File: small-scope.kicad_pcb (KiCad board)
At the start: 2 copper layers, 35.6 x 53.3 mm, 41 parts, among them P1 BNC, P2 AREF, SW1 STAT DIS, U1 LM324N

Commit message: initial placement
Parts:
- C5: value 16.9p -> 16p
- C7: value 135p -> 130p
- R1, R3, R4, R5, R6, R7, R8: footprint R4-LARGE_PADS -> R1
- moved R18 63.9 mm to (128.9, 62.2)
- moved R17 63.5 mm to (128.9, 65.4)
- moved D4 52.6 mm to (111.1, 52.1), turned to 270 degrees
- moved D2 47.2 mm to (127.0, 56.5), turned to 180 degrees
- moved SW1 43.0 mm to (34.3, 65.4)
- moved D3 42.4 mm to (106.7, 52.1), turned to 270 degrees
- moved R16 42.3 mm to (102.9, 51.4), turned to 90 degrees
- moved R11 26.9 mm to (101.6, 64.1), turned to 180 degrees
- moved JP4 26.0 mm to (111.1, 70.5)
- moved R10 25.4 mm to (127.0, 59.1), turned to 180 degrees
- moved R1 23.6 mm to (100.3, 52.1)
- moved R13 23.5 mm to (101.6, 70.5), turned to 180 degrees
- moved C7 21.0 mm to (101.6, 72.4), turned to 180 degrees
- moved C5 21.0 mm to (101.6, 68.6), turned to 0 degrees
- moved R14 20.7 mm to (101.6, 74.3), turned to 0 degrees
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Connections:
- net N-0000014 renamed /2.5V
- D4 pad 1: N-0000018 -> N-0000017
- R16 pad 1: /INFO_LED -> N-0000017
- R16 pad 2: N-0000018 -> /INFO_LED
- U1 pad 1: N-000009 -> N-0000016
- U1 pad 10: N-000004 -> /SIG_ATT
- U1 pad 12: /SIG_ATT -> N-000004
- U1 pad 13: N-000007 -> N-000005
- U1 pad 14: N-000007 -> N-000006
- U1 pad 2: N-000009 -> N-0000016
- U1 pad 3: N-0000021 -> N-0000015
- U1 pad 5: N-0000015 -> N-0000021
- U1 pad 6: N-0000016 -> N-000009
- U1 pad 7: N-0000016 -> N-000009
- U1 pad 8: N-000006 -> N-000007
- U1 pad 9: N-000005 -> N-000007
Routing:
- net /x10: track 0.00 -> 23.5 mm
- net /SIG_IN: track 0.00 -> 23.5 mm
- net /x5: track 0.00 -> 14.6 mm
- net /x20: track 0.00 -> 14.6 mm
- net /SIG_ATT: track 0.00 -> 7.62 mm
- net GND: track 4.34 -> 0.00 mm
- net VDD: track 4.34 -> 0.00 mm
- net N-0000022: track 3.18 -> 0.00 mm

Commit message: general PCB connections
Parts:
- R8: footprint R1 -> R4-LARGE_PADS
- moved SW1 59.3 mm to (93.3, 60.3)
- moved D2 10.8 mm to (116.2, 56.5), turned to 0 degrees
- moved R10 10.8 mm to (116.2, 59.1), turned to 0 degrees
- moved R8 9.03 mm to (124.5, 57.8)
- moved D3 8.13 mm to (100.3, 57.1)
- moved D4 8.13 mm to (104.8, 57.1)
- moved C2 7.96 mm to (130.2, 59.1), turned to 270 degrees
- moved R9 6.35 mm to (130.2, 88.9), turned to 225 degrees
- moved R3 3.86 mm to (128.9, 83.8)
- moved R5 2.62 mm to (125.7, 85.1), turned to 270 degrees
- moved RV1 2.54 mm to (119.4, 62.9)
- moved R18 0.64 mm to (128.9, 62.9), turned to 180 degrees
- moved C1 0.63 mm to (122.6, 87.0), turned to 270 degrees
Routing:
- net /SIG_UC: track 0.00 -> 75.4 mm
- net VDD: track 0.00 -> 34.5 mm
- net VCC: track 0.00 -> 31.5 mm, vias 0 -> 2
- net N-000009: track 0.00 -> 15.5 mm
- net /THR_IN: track 0.00 -> 13.9 mm
- net /SIG_ATT: track 7.62 -> 21.5 mm
- net /2.5V: track 0.00 -> 13.2 mm
- net N-000006: track 0.00 -> 13.1 mm
- net N-0000010: track 0.00 -> 12.6 mm
- net N-000004: track 0.00 -> 8.56 mm
- net N-000005: track 0.00 -> 8.19 mm
- net /Vin: track 0.00 -> 7.93 mm
- net N-0000015: track 0.00 -> 7.03 mm
- net N-000003: track 0.00 -> 6.46 mm
- net /THR_OUT: track 0.00 -> 5.87 mm
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- added copper zone on B.Cu, net GND

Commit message: routing done
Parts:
- P1: footprint SIL-2 -> BNCv
- moved P1 21.1 mm to (99.1, 88.3), turned to 135 degrees
- moved JP2 3.42 mm to (114.9, 84.5), turned to 180 degrees
- moved R3 1.80 mm to (127.6, 85.1)
- moved SW1 1.80 mm to (94.6, 59.1)
- moved R2 1.27 mm to (121.9, 79.4)
- moved C1 0.90 mm to (121.9, 86.4)
- moved R4 0.64 mm to (121.9, 81.9)
- moved R5 0.64 mm to (125.1, 85.1)
- moved R16 0.63 mm to (102.9, 52.1)
- turned C4 to 180 degrees
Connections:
- SHIELD1 pad GND1: GND -> (no net)
- SHIELD1 pad GND2: GND -> (no net)
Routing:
- net VCC: track 31.5 -> 82.0 mm
- net GND: track 4.34 -> 47.4 mm, vias 0 -> 6
- net /SIG_IN: track 23.5 -> 45.4 mm
- net (no net): track 0.00 -> 15.2 mm
- net VDD: track 34.5 -> 38.9 mm
- net N-000001: track 5.13 -> 7.51 mm
- net /2.5V: track 13.2 -> 10.9 mm
- net /SIG_UC: track 75.4 -> 77.0 mm
- net N-0000019: track 3.96 -> 3.33 mm
- net /INFO_LED: track 2.91 -> 3.54 mm
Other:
- board size 35.6 x 53.3 mm -> 47.6 x 53.3 mm
- board text added: "SB"
- board text added: "sinister.io"
- board text added: "small-scope"

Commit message: added AC/DC select and separate DC bias
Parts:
- added C10: 10u/35V, C1, F.Cu at (149.2, 93.3)
- added C11: 10u, C1, F.Cu at (149.2, 88.3)
- added JP5: AC/DC, SIL-3, F.Cu at (149.2, 81.3)
- added R19: 10k, R1, F.Cu at (149.9, 97.8)
- added RV2: 10k, SIL-3, F.Cu at (149.2, 75.6)
- JP2: value AC/DC -> DC BIAS
- R3, R5: value 1k -> 10k
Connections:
- C1 pad 1: /2.5V -> /BIAS
- JP2 pad 1: /2.5V -> /BIAS
- R3 pad 1: VCC -> /2.5V
- R3 pad 2: /2.5V -> N-0000019
- R5 pad 2: GND -> VCC
- U1 pad 10: /SIG_ATT -> /SIG_ACDC
- U1 pad 11: GND -> VDD
- U1 pad 4: VDD -> GND
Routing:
- net VCC: track 82.0 -> 7.40 mm, vias 2 -> 0
- net /SIG_ATT: track 21.5 -> 10.8 mm
- net /2.5V: track 10.9 -> 2.54 mm
- net VDD: track 38.9 -> 32.6 mm
- net /BIAS: track 0.00 -> 4.71 mm
- net GND: track 47.4 -> 49.4 mm

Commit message: board rev1
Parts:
- R5: footprint R1 -> R4-LARGE_PADS
- moved R19 51.7 mm to (103.5, 74.9)
- moved C10 48.7 mm to (107.3, 68.6), turned to 270 degrees
- moved C11 47.0 mm to (103.5, 77.5), turned to 180 degrees
- moved JP5 41.0 mm to (109.9, 69.8), turned to 270 degrees
- moved RV2 34.8 mm to (115.6, 84.5)
- moved R3 26.8 mm to (104.8, 71.1)
- moved R5 19.3 mm to (107.3, 77.5)
- moved C6 12.7 mm to (101.0, 69.8)
- moved R11 12.3 mm to (91.4, 57.1)
- moved C5 12.3 mm to (91.4, 61.6)
- moved C7 12.3 mm to (91.4, 65.4)
- moved C8 12.3 mm to (91.4, 69.2)
- moved C9 12.3 mm to (91.4, 73.0)
- moved JP4 12.3 mm to (101.0, 63.5)
- moved R12 12.3 mm to (91.4, 59.7)
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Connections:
- SHIELD1 pad GND1: (no net) -> GND
- SHIELD1 pad GND2: (no net) -> GND
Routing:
- net VCC: track 7.40 -> 54.9 mm, vias 0 -> 4
- net GND: track 49.4 -> 32.6 mm, vias 6 -> 0
- net (no net): track 15.2 -> 0.00 mm
- net /SIG_ACDC: track 0.00 -> 14.3 mm
- net N-000003: track 3.17 -> 10.3 mm
- net /SIG_ATT: track 10.8 -> 17.8 mm
- net VDD: track 32.6 -> 39.2 mm
- net N-0000013: track 0.00 -> 6.13 mm
- net /THR_IN: track 13.9 -> 7.77 mm
- net N-000009: track 15.5 -> 9.68 mm
- net /2.5V: track 2.54 -> 7.62 mm
- net /SIG_IN: track 45.4 -> 50.1 mm
- net N-0000011: track 6.46 -> 9.80 mm
- net N-000007: track 8.19 -> 11.5 mm
- net N-0000054: track 12.6 -> 9.53 mm
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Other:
- board size 47.6 x 53.3 mm -> 57.8 x 53.3 mm
- board text removed: "SB"

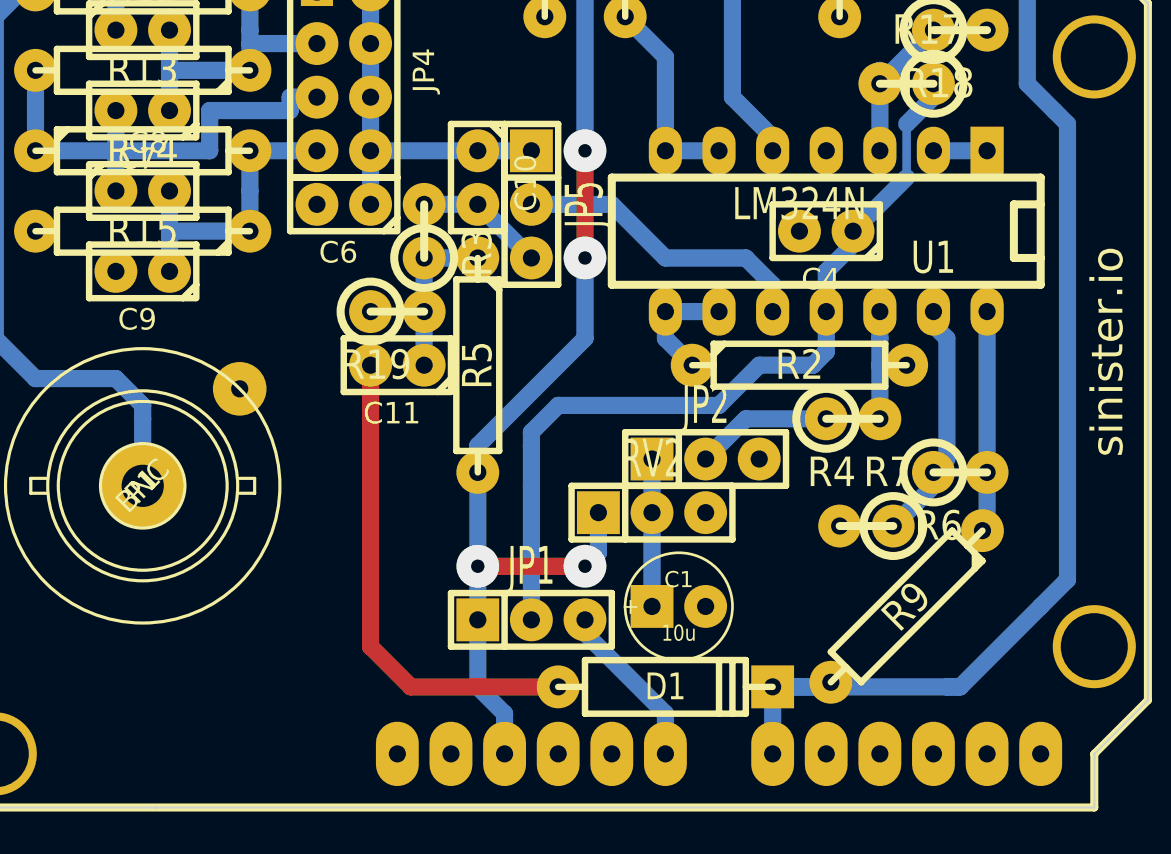
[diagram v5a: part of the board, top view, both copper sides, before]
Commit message: Fixed reversed power supply on OP amp
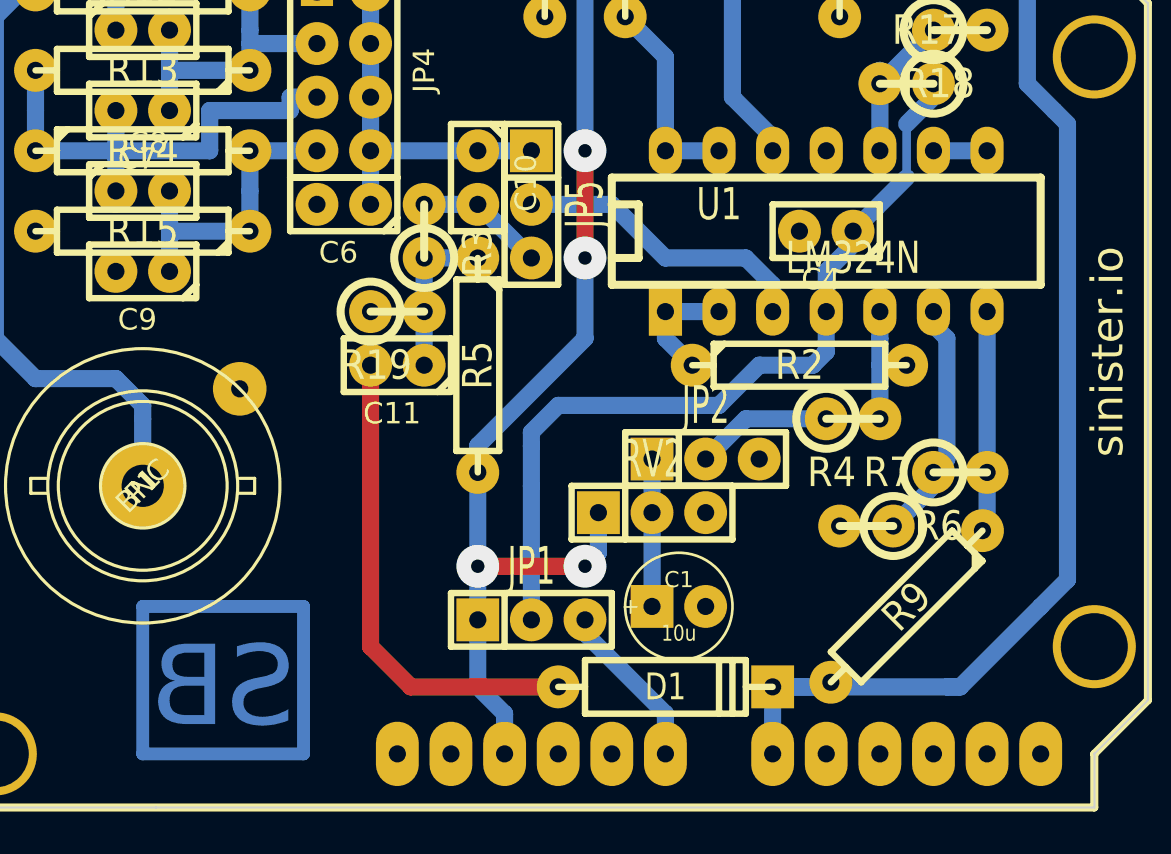
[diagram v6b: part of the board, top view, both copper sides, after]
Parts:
- turned U1 to 0 degrees
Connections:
- U1 pad 1: N-0000024 -> N-000005
- U1 pad 10: /SIG_ACDC -> N-0000018
- U1 pad 11: VDD -> GND
- U1 pad 12: N-000006 -> N-000003
- U1 pad 13: N-000007 -> N-000009
- U1 pad 14: N-000008 -> N-000009
- U1 pad 2: N-0000024 -> N-000005
- U1 pad 3: N-0000018 -> /SIG_ACDC
- U1 pad 4: GND -> VDD
- U1 pad 5: N-000003 -> N-000006
- U1 pad 6: N-000009 -> N-000007
- U1 pad 7: N-000009 -> N-000008
- U1 pad 8: N-000005 -> N-0000024
- U1 pad 9: N-000005 -> N-0000024
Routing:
- net (no net): track 0.00 -> 29.2 mm
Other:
- board text added: "SB"

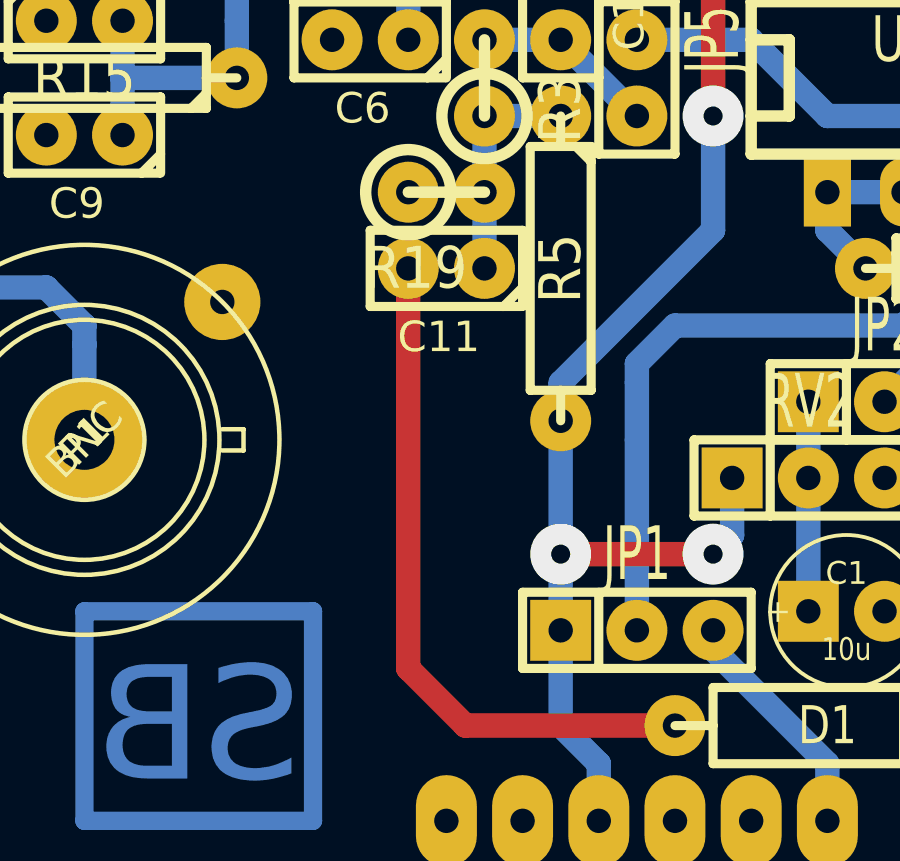
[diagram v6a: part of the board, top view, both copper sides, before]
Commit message: changed C11 footprint
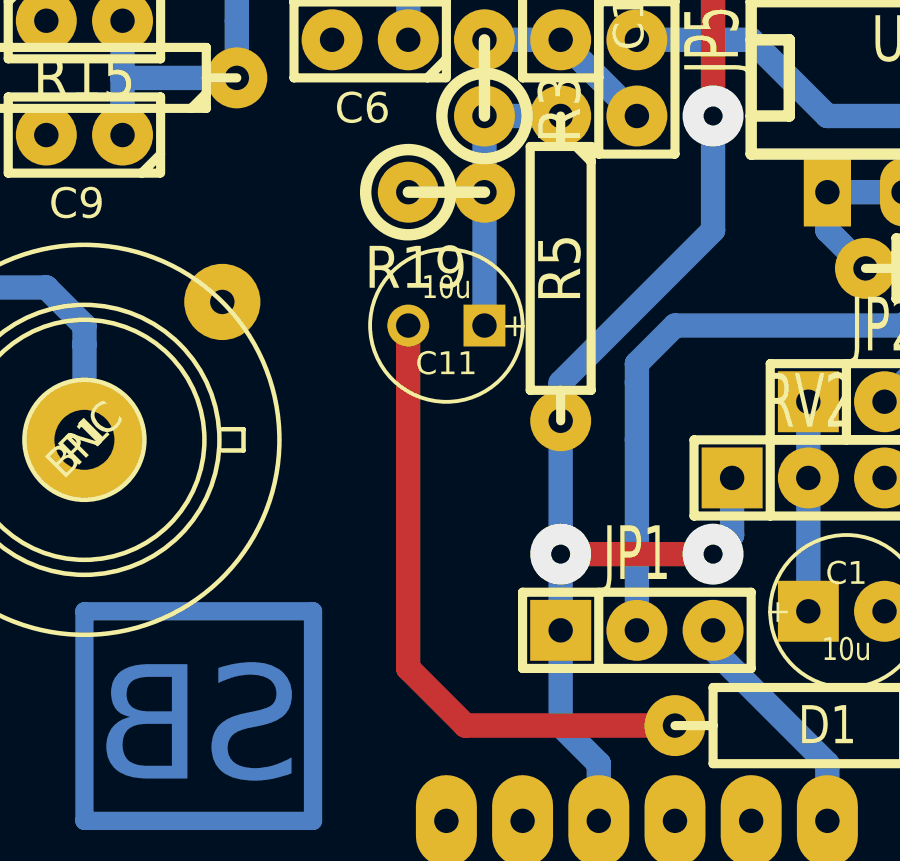
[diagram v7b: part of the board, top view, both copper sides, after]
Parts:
- C11: footprint C1 -> C1V5
- moved C11 1.91 mm to (103.5, 79.4)
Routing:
- net GND: track 32.6 -> 30.7 mm
- net /2.5V: track 7.62 -> 9.52 mm
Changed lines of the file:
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@@
-  )
-  (module C1 (layer F.Cu)
-    (at 103.505 77.47 180)
-    (descr "Condensateur e = 1 pas")
-    (tags C)
-    (fp_text reference C11 (at 0.254 -2.286 180) (layer F.SilkS)
-      (effects (font (size 1.016 1.016) (thickness 0.2032)))
-    )
-    (fp_text value 10u (at 0 -2.286 180) (layer F.SilkS) hide
-      (effects (font (size 1.016 1.016) (thickness 0.2032)))
-    )
-    (fp_line (start -2.4892 -1.27) (end 2.54 -1.27) (layer F.SilkS) (width 0.3048))
-    (fp_line (start 2.54 -1.27) (end 2.54 1.27) (layer F.SilkS) (width 0.3048))
-    (fp_line (start 2.54 1.27) (end -2.54 1.27) (layer F.SilkS) (width 0.3048))
-    (fp_line (start -2.54 1.27) (end -2.54 -1.27) (layer F.SilkS) (width 0.3048))
-    (fp_line (start -2.54 -0.635) (end -1.905 -1.27) (layer F.SilkS) (width 0.3048))
-    (pad 1 thru_hole circle (at -1.27 0 180) (size 2.032 2.032) (drill 0.8128)
-      (layers *.Cu *.Mask F.SilkS)
-      (net 1 /2.5V)
-    )
-    (pad 2 thru_hole circle (at 1.27 0 180) (size 2.032 2.032) (drill 0.8128)
-      (layers *.Cu *.Mask F.SilkS)
-      (net 15 GND)
-    )
-    (model discret/capa_1_pas.wrl
-      (at (xyz 0 0 0))
-      (scale (xyz 1 1 1))
-      (rotate (xyz 0 0 0))
-    )
   )
   (module C1 (layer F.Cu)
@@
     )
     (model discret/verti_resistor.wrl
+      (at (xyz 0 0 0))
+      (scale (xyz 1 1 1))
+      (rotate (xyz 0 0 0))
+    )
+  )
+  (module C1V5 (layer F.Cu)
+    (at 103.505 79.375 180)
+    (descr "Condensateur e = 1 pas")
+    (tags C)
+    (fp_text reference C11 (at 0 -1.26746 180) (layer F.SilkS)
+      (effects (font (size 0.762 0.762) (thickness 0.127)))
+    )
+    (fp_text value 10u (at 0 1.27 180) (layer F.SilkS)
+      (effects (font (size 0.762 0.635) (thickness 0.127)))
+    )
+    (fp_text user + (at -2.286 0 180) (layer F.SilkS)
+      (effects (font (size 0.762 0.762) (thickness 0.2032)))
+    )
+    (fp_circle (center 0 0) (end 0.127 -2.54) (layer F.SilkS) (width 0.127))
+    (pad 1 thru_hole rect (at -1.27 0 180) (size 1.397 1.397) (drill 0.8128)
+      (layers *.Cu *.Mask F.SilkS)
+      (net 1 /2.5V)
+    )
+    (pad 2 thru_hole circle (at 1.27 0 180) (size 1.397 1.397) (drill 0.8128)
+      (layers *.Cu *.Mask F.SilkS)
+      (net 15 GND)
+    )
+    (model discret/c_vert_c1v5.wrl
       (at (xyz 0 0 0))
       (scale (xyz 1 1 1))
@@
   (segment (start 99.06 95.885) (end 91.44 95.885) (width 0.6096) (layer B.Cu) (net 0))
   (segment (start 99.06 88.9) (end 99.06 95.885) (width 0.6096) (layer B.Cu) (net 0))
-  (segment (start 104.775 74.93) (end 104.775 77.47) (width 0.8128) (layer B.Cu) (net 1) (status 20))
+  (segment (start 104.775 74.93) (end 104.775 79.375) (width 0.8128) (layer B.Cu) (net 1) (status 20))
   (segment (start 104.775 72.39) (end 104.775 74.93) (width 0.8128) (layer B.Cu) (net 1) (status 20))
   (segment (start 104.775 72.39) (end 107.315 72.39) (width 0.8128) (layer B.Cu) (net 1) (status 10))
@@
   (segment (start 96.52 61.595) (end 96.52 62.23) (width 0.8128) (layer B.Cu) (net 14))
   (segment (start 96.52 62.23) (end 96.52 63.5) (width 0.8128) (layer B.Cu) (net 14))
-  (segment (start 102.235 77.47) (end 102.235 90.805) (width 0.8128) (layer F.Cu) (net 15))
+  (segment (start 102.235 79.375) (end 102.235 90.805) (width 0.8128) (layer F.Cu) (net 15) (status 10))
   (segment (start 104.14 92.71) (end 111.125 92.71) (width 0.8128) (layer F.Cu) (net 15))
   (segment (start 102.235 90.805) (end 104.14 92.71) (width 0.8128) (layer F.Cu) (net 15))
